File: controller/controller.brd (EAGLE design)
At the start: 84 x 44 mm, 47 parts, among them IC1 MEGA8-P, IC2 FT230XS, IC3 LM50, T1 2N3904, X1 MINI-USB_SHIELD5P2-32005-601, Y1 32.768kHz

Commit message: Update
Completed the controller design
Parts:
- removed IC2: FT230XS, ftdichip:SSOP16
- removed IC3: LM50, linear:SOT23
- removed Q2: (no value), crystal:HC18U-V
- removed R12: 3k3, rcl:0207/10
- removed R13: 10k, rcl:0207/10
- added C11, C20: 100n, rcl:C025-024X044
- added C19: 47u, rcl:E1,8-4
- added IC100: LM50, linear:SOT23
- added IC101: FT230XS, ftdichip:SSOP16
- added Q1: (no value), crystal:HC18U-V
- added R100, R101: 27, rcl:R0603
- C12: value 4u7 -> 10n; device rcl:E1,8-4 -> rcl:C025-024X044
- C13: value 100n -> 470n
- C14, C15: value 10n -> 100n
- C16, C4: value 100n -> 10n
- C17: value 100n -> 4u7; device rcl:C025-024X044 -> rcl:E1,8-4
- C18: value 470n -> 47u; device rcl:C025-024X044 -> rcl:E1,8-4
- C5, C7: value 47u -> 100n; device rcl:E1,8-4 -> rcl:C025-024X044
- ISP1: value AVRISP-BOX -> AVRISP-6; device adafruit:AVRISP-BOX -> adafruit:AVRISP
- R10: value 100k -> 10k; device pot:CT6 -> rcl:0207/10
- R11: value Blue/White/Green=80/Amber=180 -> 100k; device rcl:0207/10 -> pot:CT6
- R2: value 27 -> 10k; device rcl:R0603 -> rcl:0207/10
- R3: value 27 -> 3k3; device rcl:R0603 -> rcl:0207/10
- R6: value 3k3 -> Blue/White/Green=80/Amber=180
- R7: value 3k3 -> 10k
- R8, R9: value 10k -> 3k3
- moved R3 64.0 mm to (10.8, 21.6), flipped to the top, turned to 270 degrees
- moved C18 59.2 mm to (79.4, 12.1), turned to 0 degrees
- moved R6 53.1 mm to (7.62, 13.5)
- moved C13 51.8 mm to (22.9, 15.2), turned to 90 degrees
- moved R11 46.8 mm to (67.9, 5.08), turned to 90 degrees
- moved C14 46.7 mm to (25.4, 15.2)
- moved S3 45.3 mm to (50.5, 38.7), turned to 90 degrees
- moved C5 43.9 mm to (39.2, 33.9), turned to 90 degrees
- moved S1 42.7 mm to (8.89, 38.7), turned to 90 degrees
- moved C15 39.9 mm to (27.9, 15.2), turned to 270 degrees
- moved C9 39.7 mm to (66.7, 22.9), turned to 0 degrees
- moved C16 37.8 mm to (30.5, 15.2), turned to 270 degrees
- moved R7 35.5 mm to (27.9, 11.4)
- moved C6 32.4 mm to (49.5, 32.4), turned to 0 degrees
- moved C17 30.7 mm to (79.4, 16.5), turned to 0 degrees
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- renumbered X1 to USB
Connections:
- net N$12 renamed V_BUS
- net ADC0: now also IC100.2; no longer IC3.2
- net ADC1: now also R11.S; no longer R10.S
- net CONT: now also C13.1, R7.2; no longer C18.1, R13.2
- net CTS: now also IC101.6; no longer IC2.6
- net E: now also IC1.19, ISP1.3; no longer IC1.18, ISP1.1
- net GND: now also C1.2, C10.2, C11.1, C12.2, C17.-, C18.-, C19.-, C2.1, C20.2, C3.2, C5.2, C7.2, C8.1, IC100.3, IC101.13, IC101.5, R11.A, S3.3; no longer C1.1, C10.1, C12.-, C17.2, C18.2, C2.2, C3.1, C5.-, C7.-, C8.2, IC2.13, IC2.5, IC3.3, R10.A, S3.1
- net INT0: now also R2.1, RTC.3; no longer R8.2, RTC.7
- net INT1: now also R10.2, RTC.7; no longer R9.1, RTC.3
- net LIGHT: now also R3.1; no longer R12.1
- net N$1: now also C2.2, Q1.2; no longer C1.2, Q2.2
- net N$10: now also IC101.9, R100.1; no longer IC2.9, R3.1
- net N$11: now also C11.2, IC101.10, IC101.11, IC101.3; no longer C10.2, IC2.10, IC2.11, IC2.3
- net N$13: now also IC101.14; no longer IC2.14
- net N$18: now also R3.2; no longer R12.2
- net N$19: now also R6.2; no longer R11.2
- net N$2: now also C1.1, Q1.1; no longer C2.1, Q2.1
- net N$20: now also R9.2; no longer R7.2
- net N$21: now also R8.1; no longer R6.1
- net N$3: now also R100.2; no longer R3.2
- net N$4: now also C8.2; no longer C3.2
- net N$5: now also IC101.15; no longer IC2.15
- net N$6: now also R101.1; no longer R2.1
- net N$7: now also S2.3; no longer S3.3
- net N$8: now also S1.3; no longer S2.3
- net N$9: now also IC101.8, R101.2; no longer IC2.8, R2.2
- net PWM: now also R7.1; no longer R13.1
- net RESET: now also C6.1, S3.1; no longer C4.1, S1.3
- net RS: now also IC1.18, ISP1.1; no longer IC1.19, ISP1.3
- net RTS: now also IC101.2; no longer IC2.2
- net RXD: now also IC101.4; no longer IC2.4
- net TXD: now also IC101.1; no longer IC2.1
- net VCC: now also C10.1, C12.1, C17.+, C18.+, C19.+, C20.1, C3.1, C4.1, C5.1, C7.1, IC100.1, IC101.12, R10.1, R11.E, R2.2, R6.1, R8.2, R9.1; no longer C12.+, C13.1, C17.1, C5.+, C6.1, C7.+, C8.1, IC2.12, IC3.1, R10.E, R11.1, R6.2, R7.1, R8.1, R9.2
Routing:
- net DB7: track 0.00 -> 63.7 mm
- net RTS: track 0.00 -> 49.9 mm, vias 0 -> 1
- net DB4: track 0.00 -> 48.1 mm
- net RESET: track 0.00 -> 41.7 mm
- net E: track 0.00 -> 41.3 mm
- net DB6: track 0.00 -> 41.3 mm
- net DB5: track 0.00 -> 40.9 mm
- net ADC1: track 0.00 -> 40.7 mm
- net RS: track 0.00 -> 39.0 mm
- net CTS: track 0.00 -> 37.0 mm, vias 0 -> 1
- net LIGHT: track 0.00 -> 35.2 mm
- net INT1: track 0.00 -> 30.0 mm
- net RXD: track 0.00 -> 28.7 mm
- net ADC0: track 0.00 -> 28.7 mm
- net TXD: track 0.00 -> 25.8 mm
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- added copper zone on layer 1, net GND
- added copper zone on layer 16, net GND
- added copper zone on layer 1, net RESET
- added copper zone on layer 1, net VCC
- added copper zone on layer 16, net VCC
- added copper zone on layer 1, net V_BUS
- added copper zone on layer 16, net V_BUS
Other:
- board text added: "Controller"
- board text added: "G.Raf v1.0"

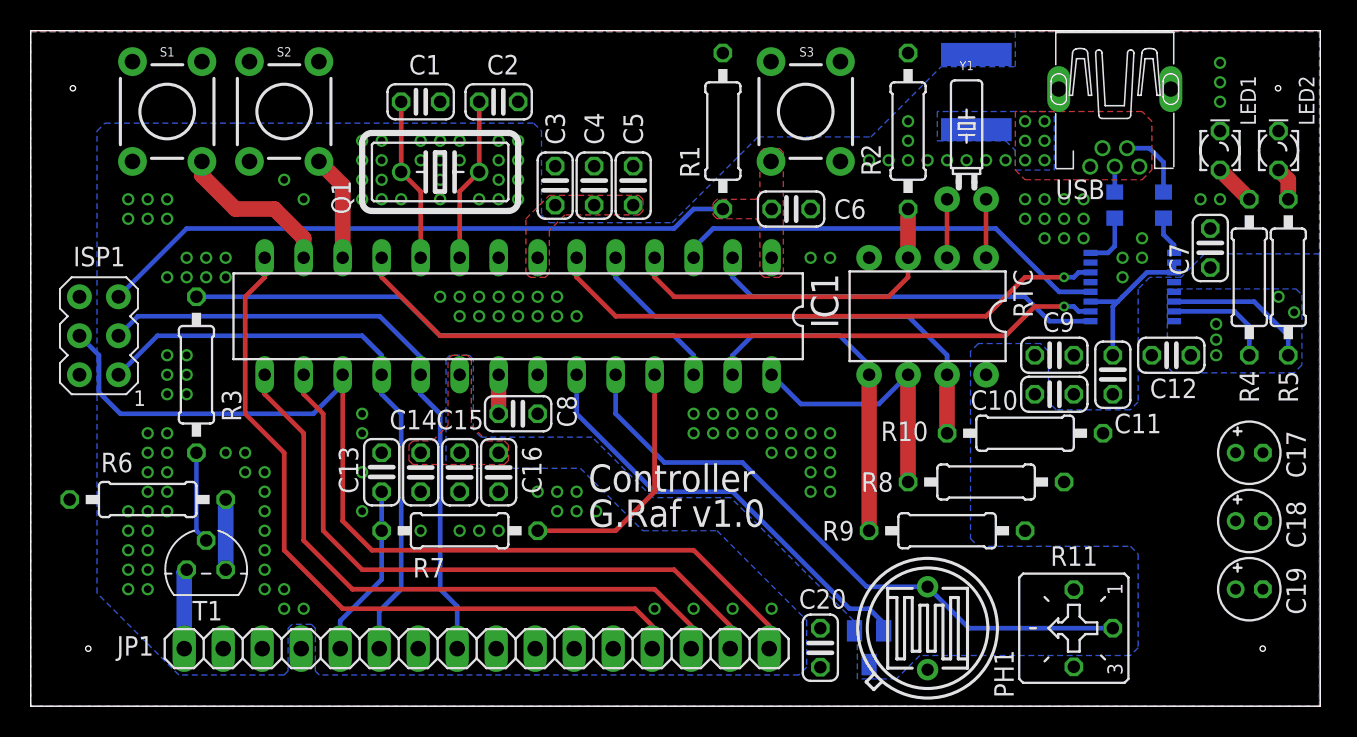
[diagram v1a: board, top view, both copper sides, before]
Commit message: Update
Corrected some things and added partlist to the controller project
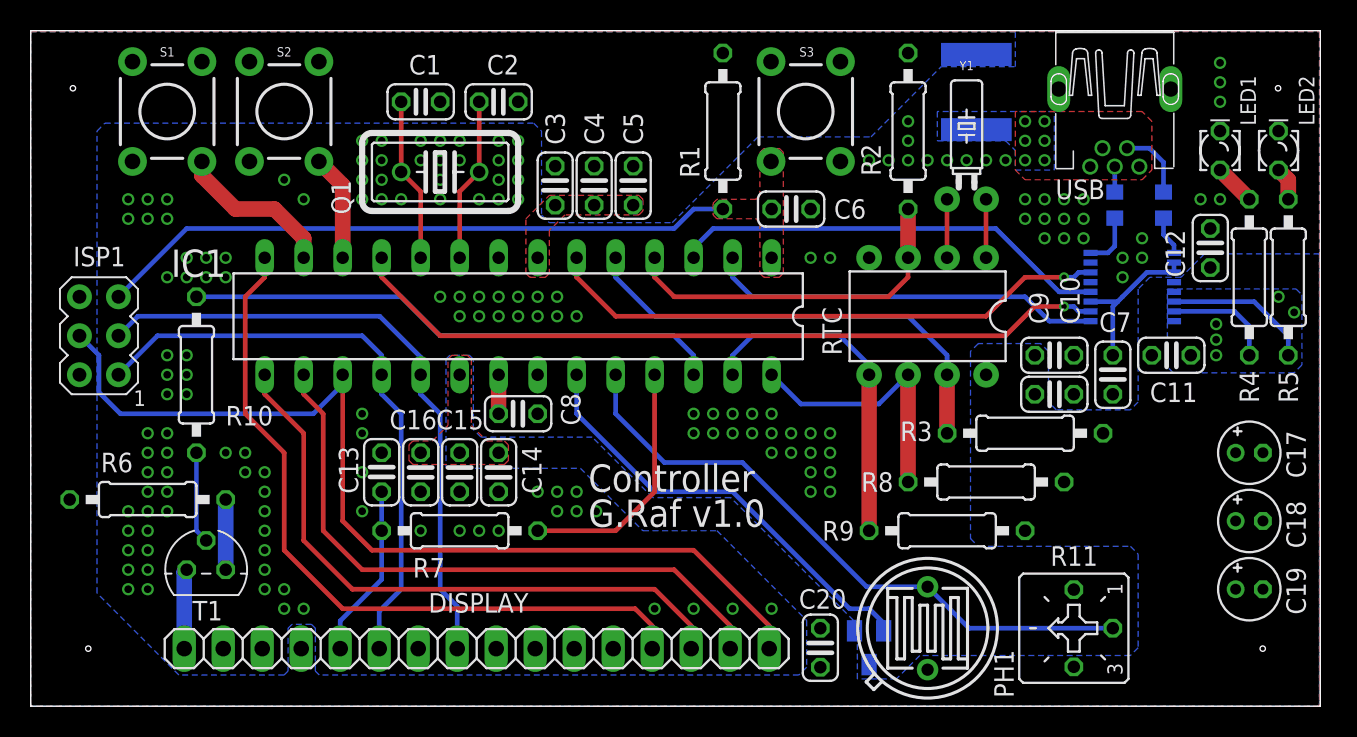
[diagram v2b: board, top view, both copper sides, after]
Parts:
- C11, C14, C3: value 100n -> 10n
- C12, C16, C4: value 10n -> 100n
- R10: value 10k -> 3k3
- R3: value 3k3 -> 10k
- moved R10 54.1 mm to (10.8, 21.6), turned to 270 degrees
- moved R3 54.1 mm to (64.8, 17.8), turned to 180 degrees
- moved C7 10.4 mm to (70.5, 21.6)
- moved C12 7.43 mm to (76.8, 29.8), turned to 90 degrees
- moved C14 5.08 mm to (30.5, 15.2)
- moved C16 5.08 mm to (25.4, 15.2)
- moved C11 4.02 mm to (74.3, 22.9), turned to 0 degrees
- renumbered IC100 to IC3, IC101 to IC2, JP1 to DISPLAY, R100 to R13, R101 to R12
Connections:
- net GND: now also C11.2, C7.1; no longer C11.1, C7.2
- net INT1: now also R3.2; no longer R10.2
- net LIGHT: now also R10.1; no longer R3.1
- net N$11: now also C7.2; no longer C11.2
- net N$18: now also R10.2; no longer R3.2
- net VCC: now also C11.1, R3.1; no longer C7.1, R10.1

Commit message: Update
Corrected wrong direction of the display header
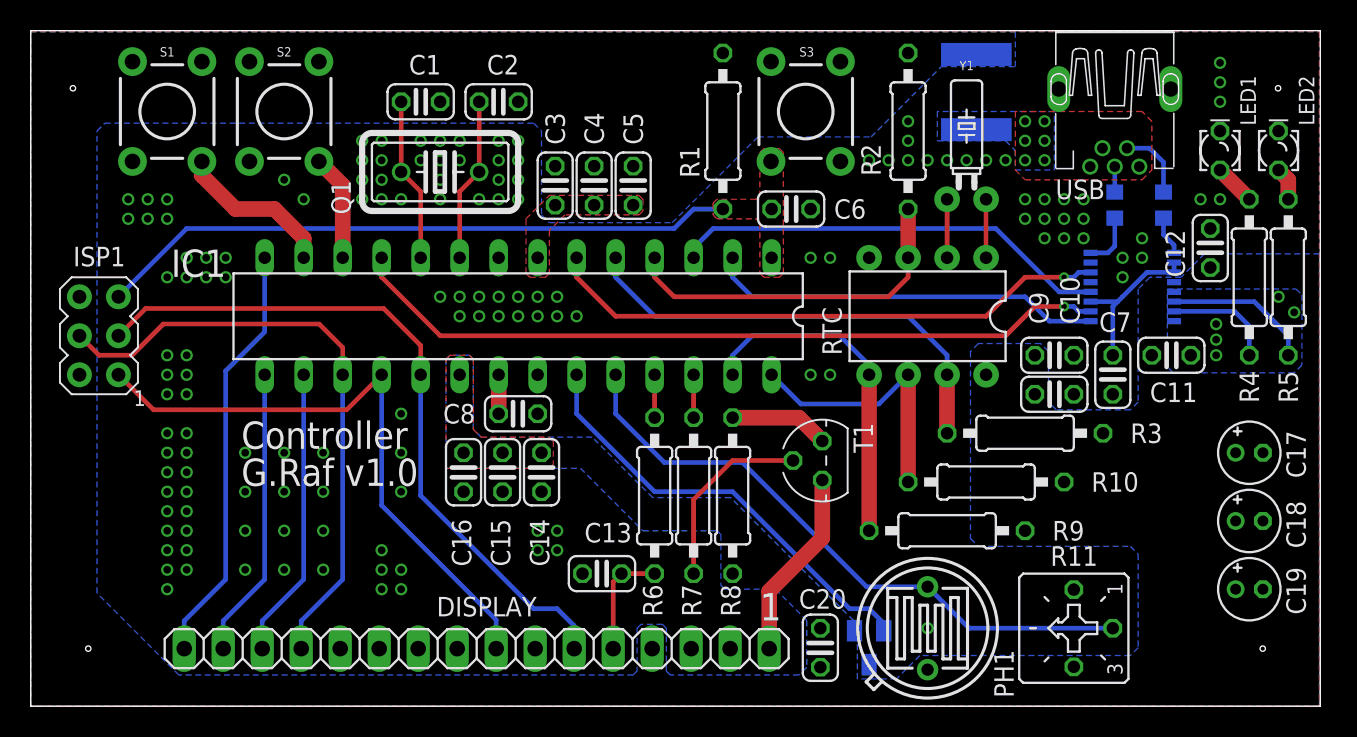
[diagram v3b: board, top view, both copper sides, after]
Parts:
- R6: value Blue/White/Green=80/Amber=180 -> 10k
- R7: value 10k -> 3k3
- R8: value 3k3 -> Blue/White/Green=80/Amber=180
- moved R10 49.9 mm to (59.7, 11.4), turned to 0 degrees
- moved T1 40.8 mm to (51.6, 16.0), turned to 90 degrees
- moved R6 33.0 mm to (40.6, 13.7), turned to 270 degrees
- moved C13 15.8 mm to (37.2, 8.64), turned to 180 degrees
- moved R7 15.4 mm to (43.2, 13.7), turned to 270 degrees
- moved R8 14.2 mm to (45.7, 13.7), turned to 90 degrees
- moved C14 2.79 mm to (33.3, 15.2)
- moved C15 2.79 mm to (30.7, 15.2)
- moved C16 2.79 mm to (28.2, 15.2)
- turned DISPLAY to 180 degrees
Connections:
- net CONT: now also R6.2; no longer R7.2
- net DB4: now also IC1.17, ISP1.4; no longer IC1.14
- net DB5: now also IC1.16; no longer IC1.15
- net DB6: now also IC1.15; no longer IC1.16
- net DB7: now also IC1.14; no longer IC1.17, ISP1.4
- net E: now also IC1.18, ISP1.1; no longer IC1.19, ISP1.3
- net LIGHT: now also R7.1; no longer R10.1
- net N$18: now also R7.2; no longer R10.2
- net N$19: now also R8.2; no longer R6.2
- net N$21: now also R10.1; no longer R8.1
- net PWM: now also R6.1; no longer R7.1
- net RS: now also IC1.19, ISP1.3; no longer IC1.18, ISP1.1
- net VCC: now also R10.2, R8.1; no longer R6.1, R8.2
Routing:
- net DB7: track 63.7 -> 27.6 mm
- net LIGHT: track 35.2 -> 2.79 mm
- net DB6: track 41.3 -> 19.0 mm
- net DB5: track 40.9 -> 19.0 mm
- net PWM: track 16.3 -> 2.79 mm
- net DB4: track 48.1 -> 39.9 mm
- net RS: track 39.0 -> 46.2 mm
- net N$16: track 5.21 -> 12.4 mm
- net N$18: track 5.98 -> 12.4 mm
- net CONT: track 11.3 -> 7.27 mm
- net N$19: track 4.57 -> 6.47 mm
- net E: track 41.3 -> 40.0 mm
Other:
- board text added: "1"
- board text added: "github.com/sunriax"
